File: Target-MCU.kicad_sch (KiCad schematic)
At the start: 18 parts, among them Q6 DMG1012UW-7, SW5 16V 50mA, U4 CH32V003F4P6

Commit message: Schematic cleanup
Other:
- note added: "RST_CH32V003"
- note added: "SWDIO_CH32V003"
- note added: "and are the output SWDIO and RST signals from the flash/debug probe. They flash new firmware to the Target MCU. TX and RX also come from the flash/debug probe. They set up a UART communication channel with the Target MCU."
- note added: "is the output RST pin from the flash/debug probe (so it's the input RST pin for the Target MCU). With this switch, you can trigger a RST manually."
- note removed: "RST_CH32V003 is the output RST pin from the flash/debug probe (so it's the input RST pin for the Target MCU). With this switch, you can trigger a RST manually."
- note removed: "SWDIO_CH32V003 and RST_CH32V003 are the output SWDIO and RST signals from the flash/debug probe. They flash new firmware to the Target MCU. TX and RX also come from the flash/debug probe. They set up a UART communication channel with the Target MCU."
- company: (none) -> Embeetle
- title: (none) -> Tiny Scarab
- moved on the sheet: C39, R25, R26, SW5, TVS9

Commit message: Apply suggestions from Petr Dvorak
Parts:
- added R30: 100k, Resistor_SMD:R_0402_1005Metric_Pad0.72x0.64mm_HandSolder, symbol Device:R
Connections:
- net GND: now also R30.1
- net PD0: now also R30.2
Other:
- moved on the sheet: R27
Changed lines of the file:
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@@
   (junction (at 95.25 34.29) (diameter 0) (color 0 0 0 0)
   )
+  (junction (at 27.94 123.19) (diameter 0) (color 0 0 0 0)
+  )
   (junction (at 38.1 107.95) (diameter 0) (color 0 0 0 0)
   )
@@
   )
   (junction (at 95.25 46.99) (diameter 0) (color 0 0 0 0)
+  )
+  (junction (at 24.13 102.87) (diameter 0) (color 0 0 0 0)
   )
   (junction (at 90.17 34.29) (diameter 0) (color 0 0 0 0)
@@
     (stroke (width 0) (type default))
   )
+  (wire (pts (xy 38.1 123.19) (xy 38.1 119.38))
+    (stroke (width 0) (type default))
+  )
   (wire (pts (xy 38.1 82.55) (xy 38.1 85.09))
     (stroke (width 0) (type default))
@@
     (stroke (width 0) (type default))
   )
+  (wire (pts (xy 24.13 102.87) (xy 16.51 102.87))
+    (stroke (width 0) (type default))
+  )
   (wire (pts (xy 38.1 109.22) (xy 38.1 107.95))
     (stroke (width 0) (type default))
@@
     (stroke (width 0) (type default))
   )
-  (wire (pts (xy 26.67 102.87) (xy 26.67 105.41))
+  (wire (pts (xy 29.21 102.87) (xy 29.21 105.41))
     (stroke (width 0) (type default))
   )
@@
     (stroke (width 0) (type default))
   )
+  (wire (pts (xy 24.13 113.03) (xy 24.13 123.19))
+    (stroke (width 0) (type default))
+  )
   (wire (pts (xy 191.77 62.23) (xy 191.77 64.77))
     (stroke (width 0) (type default))
@@
     (stroke (width 0) (type default))
   )
-  (wire (pts (xy 38.1 119.38) (xy 38.1 120.65))
+  (wire (pts (xy 27.94 123.19) (xy 27.94 125.73))
     (stroke (width 0) (type default))
   )
@@
     (stroke (width 0) (type default))
   )
-  (wire (pts (xy 26.67 114.3) (xy 26.67 113.03))
+  (wire (pts (xy 29.21 114.3) (xy 29.21 113.03))
     (stroke (width 0) (type default))
   )
@@
     (stroke (width 0) (type default))
   )
-  (wire (pts (xy 26.67 102.87) (xy 21.59 102.87))
+  (wire (pts (xy 29.21 102.87) (xy 24.13 102.87))
     (stroke (width 0) (type default))
   )
@@
     (stroke (width 0) (type default))
   )
+  (wire (pts (xy 27.94 123.19) (xy 38.1 123.19))
+    (stroke (width 0) (type default))
+  )
   (wire (pts (xy 104.14 44.45) (xy 105.41 44.45))
     (stroke (width 0) (type default))
@@
     (stroke (width 0) (type default))
   )
+  (wire (pts (xy 24.13 102.87) (xy 24.13 105.41))
+    (stroke (width 0) (type default))
+  )
   (wire (pts (xy 160.02 91.44) (xy 170.18 91.44))
     (stroke (width 0) (type default))
@@
     (stroke (width 0) (type default))
   )
+  (wire (pts (xy 24.13 123.19) (xy 27.94 123.19))
+    (stroke (width 0) (type default))
+  )
   (wire (pts (xy 160.02 86.36) (xy 170.18 86.36))
     (stroke (width 0) (type default))
@@
     (stroke (width 0) (type default))
   )
-  (wire (pts (xy 26.67 114.3) (xy 30.48 114.3))
+  (wire (pts (xy 29.21 114.3) (xy 30.48 114.3))
     (stroke (width 0) (type default))
   )
@@
     (effects (font (size 1.27 1.27)) (justify left bottom))
   )
-  (label "PD0" (at 21.59 102.87 0) (fields_autoplaced)
+  (label "PD0" (at 16.51 102.87 0) (fields_autoplaced)
     (effects (font (size 1.27 1.27)) (justify left bottom))
   )
@@
     )
   )
-  (symbol (lib_id "Device:R") (at 26.67 109.22 180) (unit 1)
-    (in_bom yes) (on_board yes) (dnp no)
-    (property "Reference" "R27" (at 26.67 109.22 90)
+  (symbol (lib_id "Device:R") (at 29.21 109.22 180) (unit 1)
+    (in_bom yes) (on_board yes) (dnp no)
+    (property "Reference" "R27" (at 29.21 109.22 90)
       (effects (font (size 1.27 1.27)))
     )
-    (property "Value" "1k" (at 29.21 109.22 0)
+    (property "Value" "1k" (at 31.75 109.22 0)
       (effects (font (size 1.27 1.27)))
     )
-    (property "Footprint" "Resistor_SMD:R_0402_1005Metric_Pad0.72x0.64mm_HandSolder" (at 28.448 109.22 90)
-      (effects (font (size 1.27 1.27)) hide)
-    )
-    (property "Datasheet" "~" (at 26.67 109.22 0)
-      (effects (font (size 1.27 1.27)) hide)
-    )
-    (property "MPN" "GPR04021K" (at 26.67 109.22 0)
+    (property "Footprint" "Resistor_SMD:R_0402_1005Metric_Pad0.72x0.64mm_HandSolder" (at 30.988 109.22 90)
+      (effects (font (size 1.27 1.27)) hide)
+    )
+    (property "Datasheet" "~" (at 29.21 109.22 0)
+      (effects (font (size 1.27 1.27)) hide)
+    )
+    (property "MPN" "GPR04021K" (at 29.21 109.22 0)
       (effects (font (size 1.27 1.27)) hide)
     )
@@
     )
   )
-  (symbol (lib_id "power:GND") (at 38.1 120.65 0) (unit 1)
-    (in_bom yes) (on_board yes) (dnp no)
-    (property "Reference" "#PWR039" (at 38.1 127 0)
-      (effects (font (size 1.27 1.27)) hide)
-    )
-    (property "Value" "GND" (at 38.1 120.65 0)
-      (effects (font (size 1.27 1.27)) (justify right))
-    )
-    (property "Footprint" "" (at 38.1 120.65 0)
-      (effects (font (size 1.27 1.27)) hide)
-    )
-    (property "Datasheet" "" (at 38.1 120.65 0)
+  (symbol (lib_id "power:GND") (at 27.94 125.73 0) (unit 1)
+    (in_bom yes) (on_board yes) (dnp no)
+    (property "Reference" "#PWR039" (at 27.94 132.08 0)
+      (effects (font (size 1.27 1.27)) hide)
+    )
+    (property "Value" "GND" (at 27.94 125.73 0)
+      (effects (font (size 1.27 1.27)) (justify left))
+    )
+    (property "Footprint" "" (at 27.94 125.73 0)
+      (effects (font (size 1.27 1.27)) hide)
+    )
+    (property "Datasheet" "" (at 27.94 125.73 0)
       (effects (font (size 1.27 1.27)) hide)
     )
@@
         )
       )
+    )
+  )
+  (symbol (lib_id "Device:R") (at 24.13 109.22 180) (unit 1)
+    (in_bom yes) (on_board yes) (dnp no)
+    (property "Reference" "R30" (at 24.13 109.22 90)
+      (effects (font (size 1.27 1.27)))
+    )
+    (property "Value" "100k" (at 21.59 109.22 90)
+      (effects (font (size 1.27 1.27)))
+    )
+    (property "Footprint" "Resistor_SMD:R_0402_1005Metric_Pad0.72x0.64mm_HandSolder" (at 25.908 109.22 90)
+      (effects (font (size 1.27 1.27)) hide)
+    )
+    (property "Datasheet" "~" (at 24.13 109.22 0)
+      (effects (font (size 1.27 1.27)) hide)
+    )
+    (property "Manufacturer" "UNI-ROYAL(Uniroyal Elec)" (at 24.13 109.22 0)
+      (effects (font (size 1.27 1.27)) hide)
+    )
+    (property "MPN" "0402WGF1003TCE" (at 24.13 109.22 90)
+      (effects (font (size 1.27 1.27)) hide)
+    )
+    (property "JLCPCB Part #" "C25741" (at 24.13 109.22 90)
+      (effects (font (size 1.27 1.27)) hide)
+    )
+    (pin "2")
+    (pin "1")
+    (instances
+      (project "tiny-scarab"
+        (path "/156c5422-ee07-49a4-8263-a2dbd26b90bd/d0c4b0c3-1e7e-4a4c-add3-8d4a3a10843d"
+          (reference "R30") (unit 1)
+        )
+      )

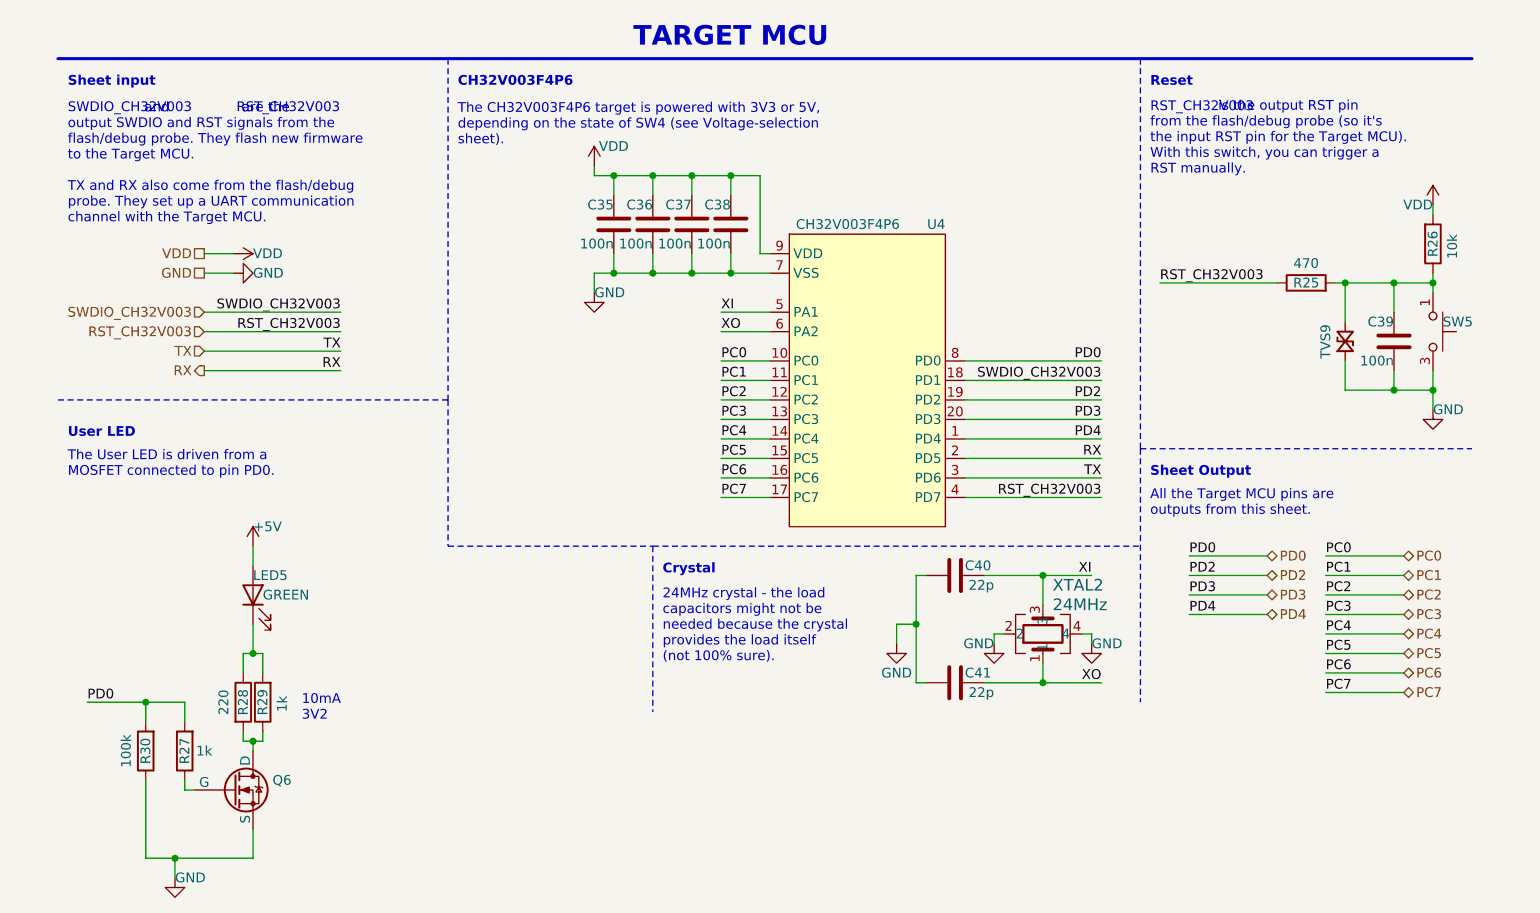
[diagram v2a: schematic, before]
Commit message: Rename capacitors
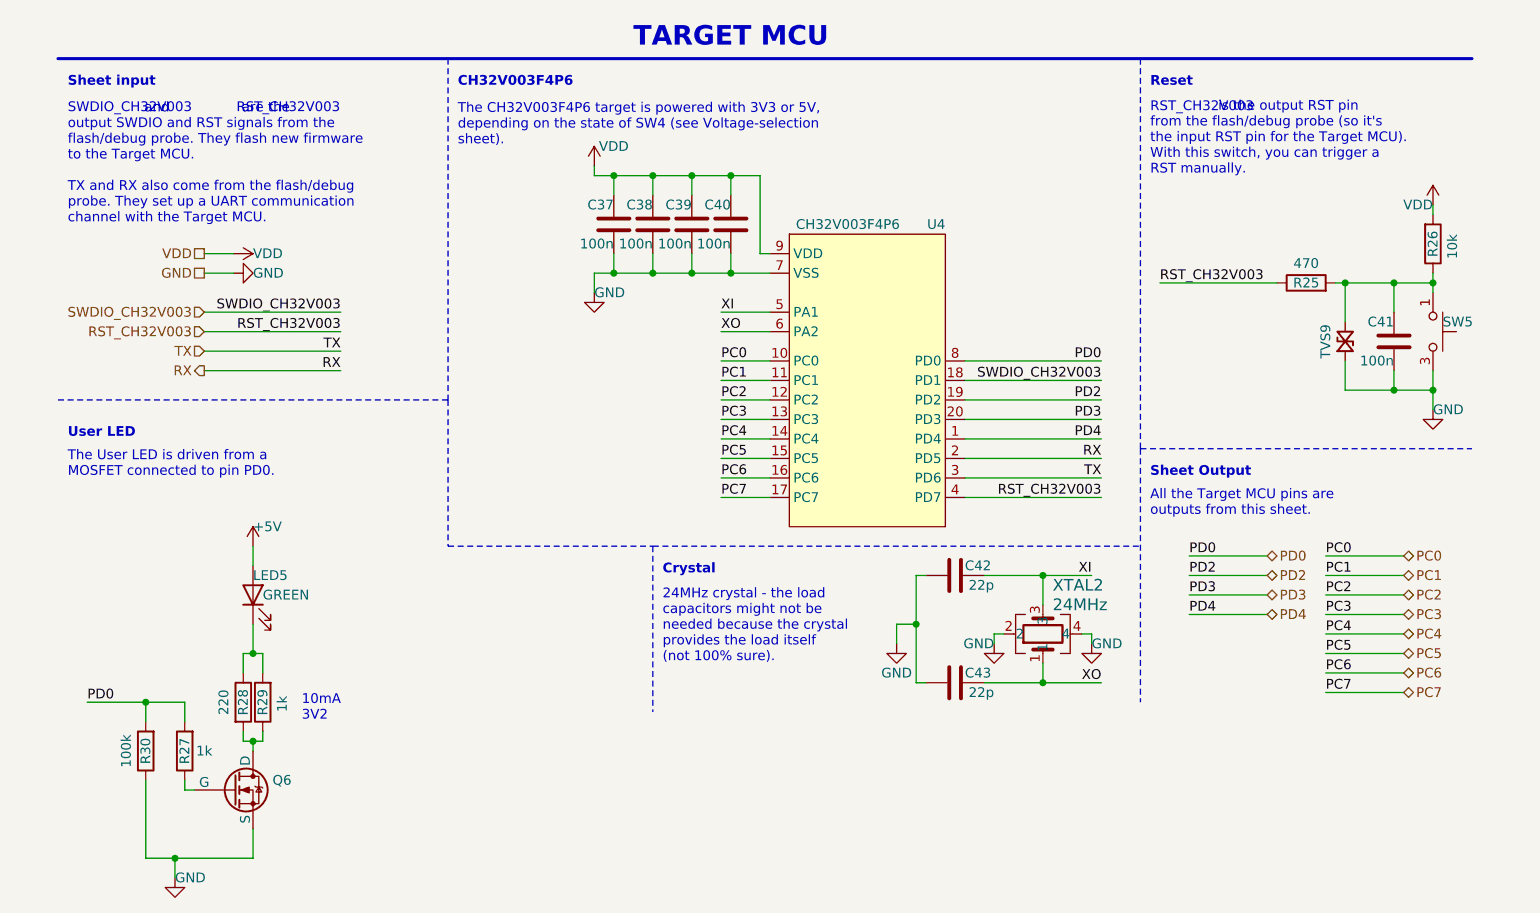
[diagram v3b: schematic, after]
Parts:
- C37: renamed from C35; Comment (none) -> 16V 100nF X7R ±10% 0402
- C38: renamed from C36; Comment (none) -> 16V 100nF X7R ±10% 0402
- C39: renamed from C37; Comment (none) -> 16V 100nF X7R ±10% 0402
- C40: renamed from C38; Comment (none) -> 16V 100nF X7R ±10% 0402
- C41: renamed from C39; Comment (none) -> 16V 100nF X7R ±10% 0402
- C42: renamed from C40; Comment (none) -> 50V 22pF C0G ±5% 0402
- C43: renamed from C41; Comment (none) -> 50V 22pF C0G ±5% 0402
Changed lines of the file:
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@@
   (symbol (lib_id "Device:C") (at 100.33 40.64 0) (mirror y) (unit 1)
     (in_bom yes) (on_board yes) (dnp no)
-    (property "Reference" "C38" (at 100.33 38.1 0)
+    (property "Reference" "C40" (at 100.33 38.1 0)
       (effects (font (size 1.27 1.27)) (justify left))
     )
@@
       (effects (font (size 1.27 1.27)) hide)
     )
-    (pin "1")
-    (pin "2")
-    (instances
-      (project "tiny-scarab"
-        (path "/156c5422-ee07-49a4-8263-a2dbd26b90bd/d0c4b0c3-1e7e-4a4c-add3-8d4a3a10843d"
-          (reference "C38") (unit 1)
+    (property "Comment" "16V 100nF X7R ±10% 0402" (at 100.33 40.64 0)
+      (effects (font (size 1.27 1.27)) hide)
+    )
+    (pin "1")
+    (pin "2")
+    (instances
+      (project "tiny-scarab"
+        (path "/156c5422-ee07-49a4-8263-a2dbd26b90bd/d0c4b0c3-1e7e-4a4c-add3-8d4a3a10843d"
+          (reference "C40") (unit 1)
         )
       )
@@
   (symbol (lib_id "Device:C") (at 129.54 100.33 90) (unit 1)
     (in_bom yes) (on_board yes) (dnp no)
-    (property "Reference" "C41" (at 130.81 99.06 90)
+    (property "Reference" "C43" (at 130.81 99.06 90)
       (effects (font (size 1.27 1.27)) (justify right))
     )
@@
       (effects (font (size 1.27 1.27)) hide)
     )
-    (pin "1")
-    (pin "2")
-    (instances
-      (project "tiny-scarab"
-        (path "/156c5422-ee07-49a4-8263-a2dbd26b90bd/d0c4b0c3-1e7e-4a4c-add3-8d4a3a10843d"
-          (reference "C41") (unit 1)
+    (property "Comment" "50V 22pF C0G ±5% 0402" (at 129.54 100.33 90)
+      (effects (font (size 1.27 1.27)) hide)
+    )
+    (pin "1")
+    (pin "2")
+    (instances
+      (project "tiny-scarab"
+        (path "/156c5422-ee07-49a4-8263-a2dbd26b90bd/d0c4b0c3-1e7e-4a4c-add3-8d4a3a10843d"
+          (reference "C43") (unit 1)
         )
       )
@@
   (symbol (lib_id "Device:C") (at 95.25 40.64 0) (mirror y) (unit 1)
     (in_bom yes) (on_board yes) (dnp no)
-    (property "Reference" "C37" (at 95.25 38.1 0)
+    (property "Reference" "C39" (at 95.25 38.1 0)
       (effects (font (size 1.27 1.27)) (justify left))
     )
@@
       (effects (font (size 1.27 1.27)) hide)
     )
-    (pin "1")
-    (pin "2")
-    (instances
-      (project "tiny-scarab"
-        (path "/156c5422-ee07-49a4-8263-a2dbd26b90bd/d0c4b0c3-1e7e-4a4c-add3-8d4a3a10843d"
-          (reference "C37") (unit 1)
+    (property "Comment" "16V 100nF X7R ±10% 0402" (at 95.25 40.64 0)
+      (effects (font (size 1.27 1.27)) hide)
+    )
+    (pin "1")
+    (pin "2")
+    (instances
+      (project "tiny-scarab"
+        (path "/156c5422-ee07-49a4-8263-a2dbd26b90bd/d0c4b0c3-1e7e-4a4c-add3-8d4a3a10843d"
+          (reference "C39") (unit 1)
         )
       )
@@
   (symbol (lib_id "Device:C") (at 90.17 40.64 0) (mirror y) (unit 1)
     (in_bom yes) (on_board yes) (dnp no)
-    (property "Reference" "C36" (at 90.17 38.1 0)
+    (property "Reference" "C38" (at 90.17 38.1 0)
       (effects (font (size 1.27 1.27)) (justify left))
     )
@@
       (effects (font (size 1.27 1.27)) hide)
     )
-    (pin "1")
-    (pin "2")
-    (instances
-      (project "tiny-scarab"
-        (path "/156c5422-ee07-49a4-8263-a2dbd26b90bd/d0c4b0c3-1e7e-4a4c-add3-8d4a3a10843d"
-          (reference "C36") (unit 1)
+    (property "Comment" "16V 100nF X7R ±10% 0402" (at 90.17 40.64 0)
+      (effects (font (size 1.27 1.27)) hide)
+    )
+    (pin "1")
+    (pin "2")
+    (instances
+      (project "tiny-scarab"
+        (path "/156c5422-ee07-49a4-8263-a2dbd26b90bd/d0c4b0c3-1e7e-4a4c-add3-8d4a3a10843d"
+          (reference "C38") (unit 1)
         )
       )
@@
   (symbol (lib_id "Device:C") (at 186.69 55.88 0) (mirror y) (unit 1)
     (in_bom yes) (on_board yes) (dnp no)
-    (property "Reference" "C39" (at 186.69 53.34 0)
+    (property "Reference" "C41" (at 186.69 53.34 0)
       (effects (font (size 1.27 1.27)) (justify left))
     )
@@
       (effects (font (size 1.27 1.27)) hide)
     )
-    (pin "1")
-    (pin "2")
-    (instances
-      (project "tiny-scarab"
-        (path "/156c5422-ee07-49a4-8263-a2dbd26b90bd/d0c4b0c3-1e7e-4a4c-add3-8d4a3a10843d"
-          (reference "C39") (unit 1)
+    (property "Comment" "16V 100nF X7R ±10% 0402" (at 186.69 55.88 0)
+      (effects (font (size 1.27 1.27)) hide)
+    )
+    (pin "1")
+    (pin "2")
+    (instances
+      (project "tiny-scarab"
+        (path "/156c5422-ee07-49a4-8263-a2dbd26b90bd/d0c4b0c3-1e7e-4a4c-add3-8d4a3a10843d"
+          (reference "C41") (unit 1)
         )
       )
@@
   (symbol (lib_id "Device:C") (at 85.09 40.64 0) (mirror y) (unit 1)
     (in_bom yes) (on_board yes) (dnp no)
-    (property "Reference" "C35" (at 85.09 38.1 0)
+    (property "Reference" "C37" (at 85.09 38.1 0)
       (effects (font (size 1.27 1.27)) (justify left))
     )
@@
       (effects (font (size 1.27 1.27)) hide)
     )
-    (pin "1")
-    (pin "2")
-    (instances
-      (project "tiny-scarab"
-        (path "/156c5422-ee07-49a4-8263-a2dbd26b90bd/d0c4b0c3-1e7e-4a4c-add3-8d4a3a10843d"
-          (reference "C35") (unit 1)
+    (property "Comment" "16V 100nF X7R ±10% 0402" (at 85.09 40.64 0)
+      (effects (font (size 1.27 1.27)) hide)
+    )
+    (pin "1")
+    (pin "2")
+    (instances
+      (project "tiny-scarab"
+        (path "/156c5422-ee07-49a4-8263-a2dbd26b90bd/d0c4b0c3-1e7e-4a4c-add3-8d4a3a10843d"
+          (reference "C37") (unit 1)
         )
       )
@@
   (symbol (lib_id "Device:C") (at 129.54 86.36 90) (unit 1)
     (in_bom yes) (on_board yes) (dnp no)
-    (property "Reference" "C40" (at 130.81 85.09 90)
+    (property "Reference" "C42" (at 130.81 85.09 90)
       (effects (font (size 1.27 1.27)) (justify right))
     )
@@
       (effects (font (size 1.27 1.27)) hide)
     )
-    (pin "1")
-    (pin "2")
-    (instances
-      (project "tiny-scarab"
-        (path "/156c5422-ee07-49a4-8263-a2dbd26b90bd/d0c4b0c3-1e7e-4a4c-add3-8d4a3a10843d"
-          (reference "C40") (unit 1)
-        )
-      )
+    (property "Comment" "50V 22pF C0G ±5% 0402" (at 129.54 86.36 90)
+      (effects (font (size 1.27 1.27)) hide)
+    )
+    (pin "1")
+    (pin "2")
+    (instances
+      (project "tiny-scarab"
+        (path "/156c5422-ee07-49a4-8263-a2dbd26b90bd/d0c4b0c3-1e7e-4a4c-add3-8d4a3a10843d"
+          (reference "C42") (unit 1)
+        )
+      )

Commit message: Add production files
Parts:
- U4: SPN 1005005036714708 -> (none); Supplier AliExpress -> (none)
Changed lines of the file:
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@@
     (effects (font (size 1.27 1.27)) (justify left bottom))
   )
-  (text "10mA\n3V2" (at 44.45 105.41 0)
+  (text "10mA\n3V2" (at 43.18 104.14 0)
     (effects (font (size 1.27 1.27)) (justify left bottom))
   )
@@
       (effects (font (size 1.27 1.27)) hide)
     )
-    (property "Supplier" "AliExpress" (at 118.11 57.15 0)
-      (effects (font (size 1.27 1.27)) hide)
-    )
-    (property "SPN" "1005005036714708" (at 118.11 57.15 0)
-      (effects (font (size 1.27 1.27)) hide)
-    )
